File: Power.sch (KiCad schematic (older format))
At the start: 20 parts, among them J6 Conn_01x02, J7 Conn_02x04_Top_Bottom, SW2 SW_SPST, U1 NJM4580, U2 NJM4580, U3 NJM4580

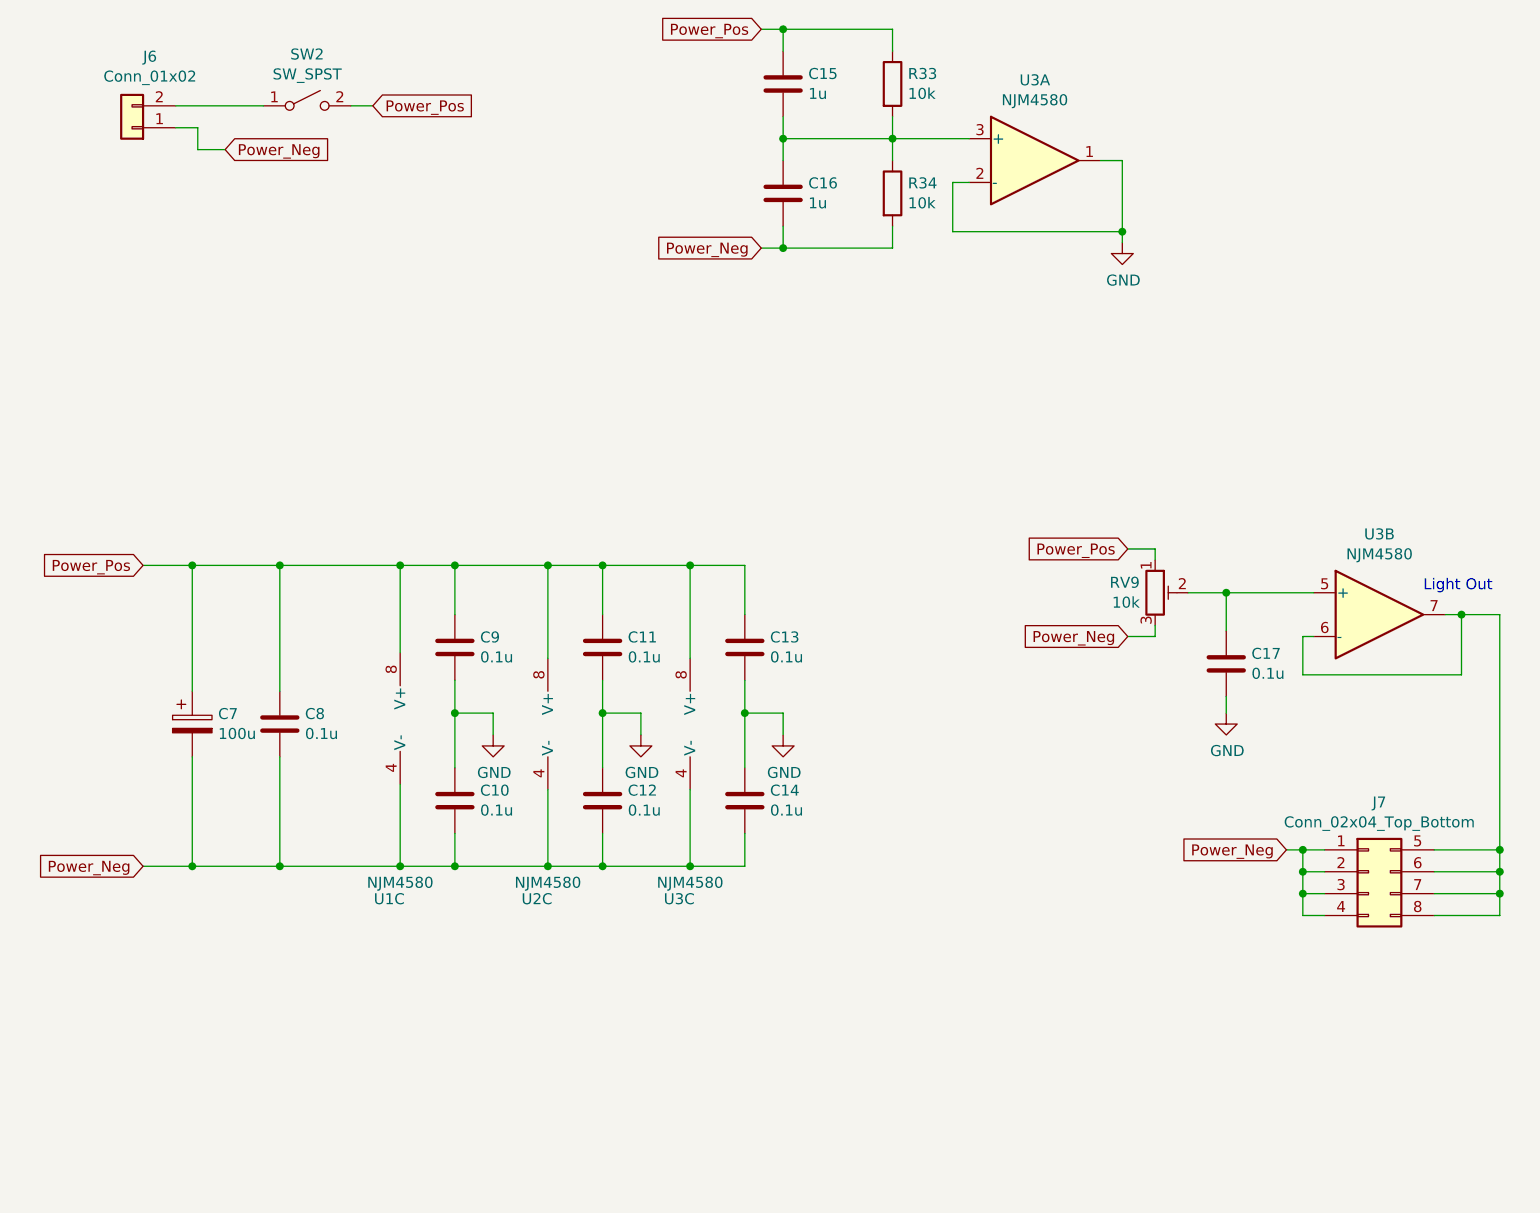
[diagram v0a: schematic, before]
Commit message: delete light
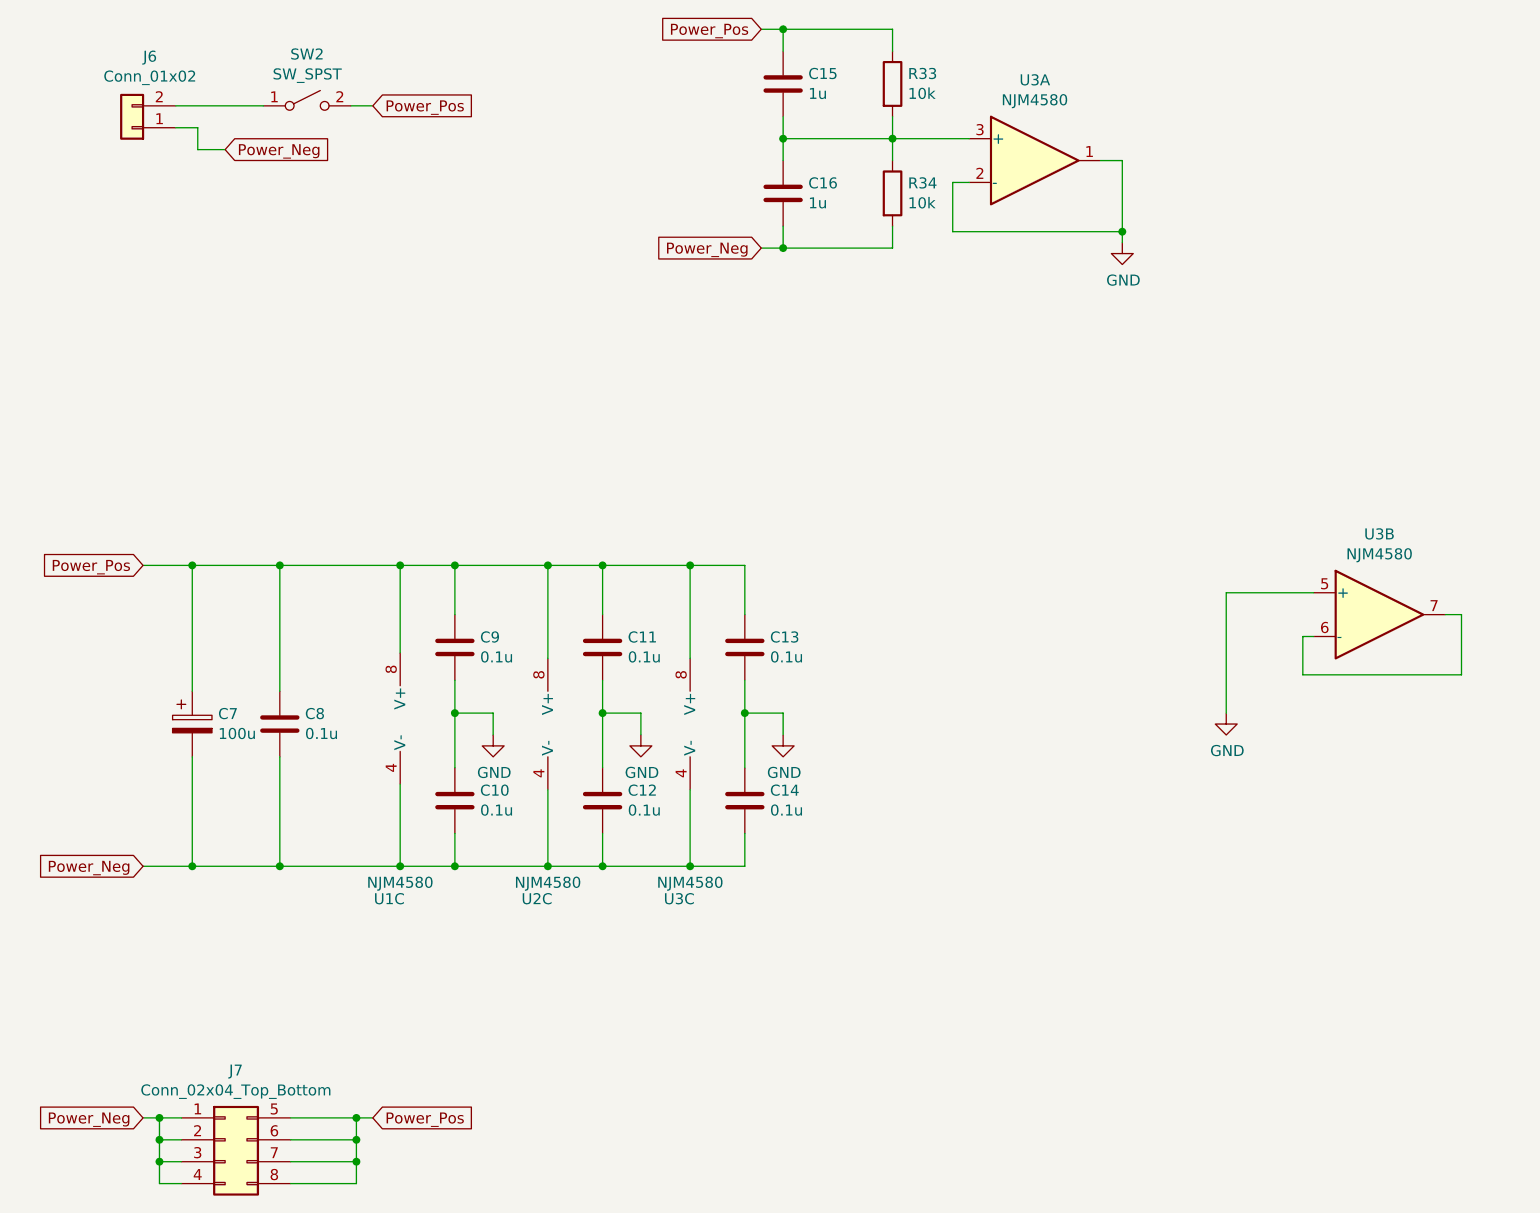
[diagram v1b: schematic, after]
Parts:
- removed C17: 0.1u, Capacitor_SMD:C_0603_1608Metric_Pad1.05x0.95mm_HandSolder, symbol Device:C
- removed RV9: 10k, Potentiometer_THT:Potentiometer_Bourns_3296W_Vertical, symbol Device:R_POT_TRIM
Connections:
- net GND: now also U3.5 (+)
- net Power_Pos: now also J7.5 (Pin_5), J7.6 (Pin_6), J7.7 (Pin_7), J7.8 (Pin_8)
- new net: U3.6 (-), U3.7
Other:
- note removed: "Light Out"
- moved on the sheet: J7
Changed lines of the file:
@@
 Wire Wire Line
 	8300 3875 8225 3875
-Wire Wire Line
-	7050 3775 7225 3775
-$Comp
-L Device:R_POT_TRIM RV?
-U 1 1 5FF19935
-P 6900 3775
-AR Path="/5FF19935" Ref="RV?"  Part="1"
-AR Path="/5FED81BD/5FF19935" Ref="RV9"  Part="1"
-F 0 "RV9" H 6830 3821 50  0000 R CNN
-F 1 "10k" H 6830 3730 50  0000 R CNN
-F 2 "Potentiometer_THT:Potentiometer_Bourns_3296W_Vertical" H 6900 3775 50  0001 C CNN
-F 3 "~" H 6900 3775 50  0001 C CNN
-	1    6900 3775
-	1    0    0    -1
-$EndComp
-Text GLabel 6775 3975 0    50   Input ~ 0
-Power_Neg
-Text GLabel 6775 3575 0    50   Input ~ 0
-Power_Pos
-Wire Wire Line
-	6775 3575 6900 3575
-Wire Wire Line
-	6900 3575 6900 3625
-Wire Wire Line
-	6775 3975 6900 3975
-Wire Wire Line
-	6900 3975 6900 3925
-$Comp
-L Connector_Generic:Conn_02x04_Top_Bottom J?
-U 1 1 5FF19941
-P 7875 5050
-AR Path="/5FF19941" Ref="J?"  Part="1"
-AR Path="/5FED81BD/5FF19941" Ref="J7"  Part="1"
-F 0 "J7" H 7925 5367 50  0000 C CNN
-F 1 "Conn_02x04_Top_Bottom" H 7925 5276 50  0000 C CNN
-F 2 "Connector_PinSocket_2.54mm:PinSocket_2x04_P2.54mm_Vertical" H 7875 5050 50  0001 C CNN
-F 3 "~" H 7875 5050 50  0001 C CNN
-	1    7875 5050
-	1    0    0    -1
-$EndComp
-Text GLabel 7500 4950 0    50   Input ~ 0
-Power_Neg
-Wire Wire Line
-	7500 4950 7575 4950
-Wire Wire Line
-	7675 5250 7575 5250
-Wire Wire Line
-	7575 5250 7575 5150
-Connection ~ 7575 4950
-Wire Wire Line
-	7575 4950 7675 4950
-Wire Wire Line
-	7675 5050 7575 5050
-Connection ~ 7575 5050
-Wire Wire Line
-	7575 5050 7575 4950
-Wire Wire Line
-	7675 5150 7575 5150
-Connection ~ 7575 5150
-Wire Wire Line
-	7575 5150 7575 5050
-Wire Wire Line
-	8300 3875 8475 3875
-Wire Wire Line
-	8475 3875 8475 4950
-Wire Wire Line
-	8475 4950 8175 4950
-Connection ~ 8300 3875
-Wire Wire Line
-	8175 5050 8475 5050
-Wire Wire Line
-	8475 5050 8475 4950
-Connection ~ 8475 4950
-Wire Wire Line
-	8175 5150 8475 5150
-Wire Wire Line
-	8475 5150 8475 5050
-Connection ~ 8475 5050
-Wire Wire Line
-	8175 5250 8475 5250
-Wire Wire Line
-	8475 5250 8475 5150
-Connection ~ 8475 5150
-Text Notes 8125 3775 0    50   ~ 0
-Light Out
-$Comp
-L Device:C C17
-U 1 1 600ADE6E
-P 7225 4100
-F 0 "C17" H 7340 4146 50  0000 L CNN
-F 1 "0.1u" H 7340 4055 50  0000 L CNN
-F 2 "Capacitor_SMD:C_0603_1608Metric_Pad1.05x0.95mm_HandSolder" H 7263 3950 50  0001 C CNN
-F 3 "~" H 7225 4100 50  0001 C CNN
-	1    7225 4100
-	1    0    0    -1
-$EndComp
 $Comp
 L power:GND #PWR022
@@
 	1    0    0    -1
 $EndComp
-Wire Wire Line
-	7225 4325 7225 4250
-Wire Wire Line
-	7225 3950 7225 3775
-Connection ~ 7225 3775
-Wire Wire Line
-	7225 3775 7625 3775
 $Comp
 L Device:C C9
@@
 Wire Wire Line
 	2525 1750 2650 1750
+Wire Wire Line
+	2950 6475 3250 6475
+Wire Wire Line
+	3250 6475 3250 6375
+Connection ~ 3250 6375
+Wire Wire Line
+	2950 6375 3250 6375
+Wire Wire Line
+	3250 6375 3250 6275
+Wire Wire Line
+	3250 6275 3250 6175
+Connection ~ 3250 6275
+Wire Wire Line
+	2950 6275 3250 6275
+Wire Wire Line
+	3250 6175 2950 6175
+Wire Wire Line
+	2450 6375 2350 6375
+Wire Wire Line
+	2350 6375 2350 6275
+Wire Wire Line
+	2350 6275 2350 6175
+Connection ~ 2350 6275
+Wire Wire Line
+	2450 6275 2350 6275
+Wire Wire Line
+	2350 6175 2450 6175
+Connection ~ 2350 6375
+Wire Wire Line
+	2350 6475 2350 6375
+Wire Wire Line
+	2450 6475 2350 6475
+Connection ~ 2350 6175
+Wire Wire Line
+	2275 6175 2350 6175
+Text GLabel 2275 6175 0    50   Input ~ 0
+Power_Neg
+$Comp
+L Connector_Generic:Conn_02x04_Top_Bottom J?
+U 1 1 5FF19941
+P 2650 6275
+AR Path="/5FF19941" Ref="J?"  Part="1"
+AR Path="/5FED81BD/5FF19941" Ref="J7"  Part="1"
+F 0 "J7" H 2700 6592 50  0000 C CNN
+F 1 "Conn_02x04_Top_Bottom" H 2700 6501 50  0000 C CNN
+F 2 "Connector_PinSocket_2.54mm:PinSocket_2x04_P2.54mm_Vertical" H 2650 6275 50  0001 C CNN
+F 3 "~" H 2650 6275 50  0001 C CNN
+	1    2650 6275
+	1    0    0    -1
+$EndComp
+Wire Wire Line
+	7225 3775 7625 3775
+Wire Wire Line
+	7225 3775 7225 4325
+Text GLabel 3325 6175 2    50   Input ~ 0
+Power_Pos
+Wire Wire Line
+	3325 6175 3250 6175
+Connection ~ 3250 6175
 $EndSCHEMATC
